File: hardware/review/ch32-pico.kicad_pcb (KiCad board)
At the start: 4 copper layers, 21 x 51 mm, 55 parts, among them J1 PICO 40-PIN, J2 GT-USB-7010AW, SW1 RESET, SW2 BOOT, U1 CH32X035C8T6, U3 TPS259470LRPWR, U4 AP63203WU-7

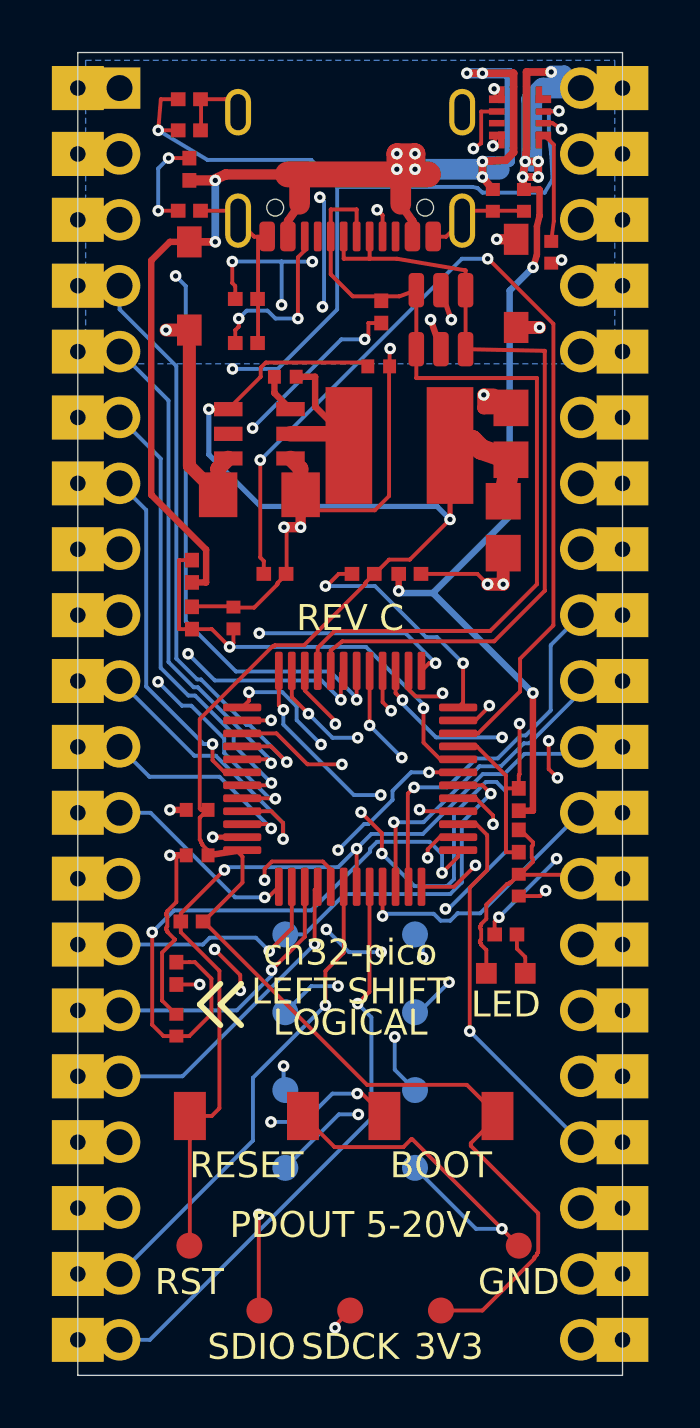
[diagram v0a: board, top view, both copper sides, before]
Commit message: Add pin 37 regulator enable control in Rev D
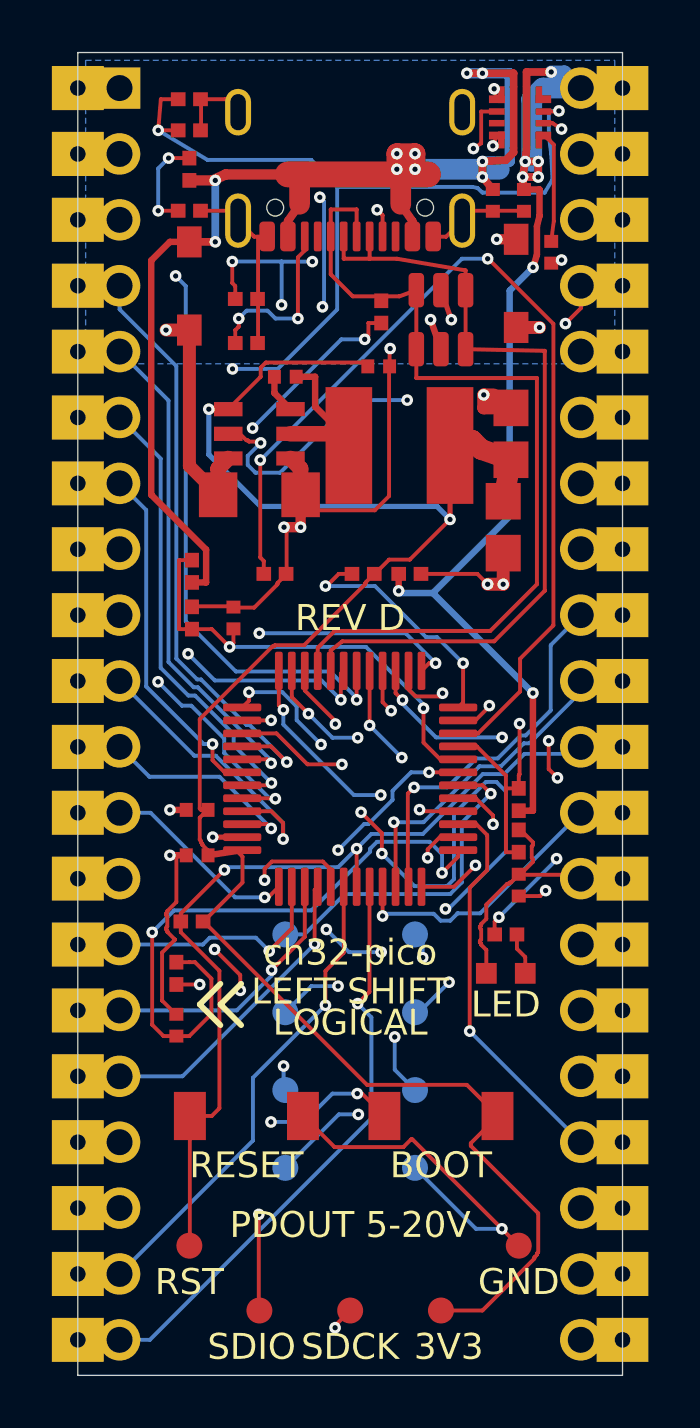
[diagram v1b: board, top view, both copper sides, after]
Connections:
- J1 pad 37: (no net) -> 3V3_EN
- U4 pad 2: (no net) -> 3V3_EN
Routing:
- net 3V3_EN: track 0.00 -> 18.9 mm, vias 0 -> 3
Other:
- board text added: "EN"
- board text added: "REV D"
- board text removed: "REV C"
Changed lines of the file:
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@@
 			(layers "*.Cu" "*.Mask")
 			(remove_unused_layers no)
+			(net "3V3_EN")
 		)
 		(pad "37" thru_hole rect
@@
 			(layers "*.Cu" "*.Mask")
 			(remove_unused_layers no)
+			(net "3V3_EN")
 		)
 		(pad "38" thru_hole circle
@@
 			(size 0.55 1.1)
 			(layers "F.Cu" "F.Mask" "F.Paste")
+			(net "3V3_EN")
 		)
 		(pad "3" smd rect
@@
 		)
 	)
-	(gr_text "REV C"
+	(gr_text "REV D"
 		(at 10.5 21.8 0)
 		(layer "F.SilkS")
@@
 		)
 	)
-	(gr_text "NC"
+	(gr_text "EN"
 		(at 16.6 8.99 0)
 		(layer "B.SilkS")
@@
 	)
 	(segment
+		(start 18.8 10.45)
+		(end 19.4 9.85)
+		(width 0.15)
+		(layer "F.Cu")
+		(net "3V3_EN")
+	)
+	(segment
+		(start 5.95 14.55)
+		(end 6.1 14.55)
+		(width 0.15)
+		(layer "F.Cu")
+		(net "3V3_EN")
+	)
+	(segment
+		(start 6.5 14.95)
+		(end 6.55 14.95)
+		(width 0.15)
+		(layer "F.Cu")
+		(net "3V3_EN")
+	)
+	(segment
+		(start 19.4 9.85)
+		(end 19.4 9)
+		(width 0.15)
+		(layer "F.Cu")
+		(net "3V3_EN")
+	)
+	(segment
+		(start 6.1 14.55)
+		(end 6.5 14.95)
+		(width 0.15)
+		(layer "F.Cu")
+		(net "3V3_EN")
+	)
+	(segment
+		(start 6.55 14.95)
+		(end 6.6 15)
+		(width 0.15)
+		(layer "F.Cu")
+		(net "3V3_EN")
+	)
+	(segment
+		(start 6.6 15)
+		(end 7 15)
+		(width 0.15)
+		(layer "F.Cu")
+		(net "3V3_EN")
+	)
+	(segment
+		(start 5.8 14.7)
+		(end 5.95 14.55)
+		(width 0.15)
+		(layer "F.Cu")
+		(net "3V3_EN")
+	)
+	(via
+		(at 12.7 13.4)
+		(size 0.45)
+		(drill 0.2)
+		(layers "F.Cu" "B.Cu")
+		(net "3V3_EN")
+	)
+	(via
+		(at 18.8 10.45)
+		(size 0.45)
+		(drill 0.2)
+		(layers "F.Cu" "B.Cu")
+		(net "3V3_EN")
+	)
+	(via
+		(at 7.05 15.05)
+		(size 0.45)
+		(drill 0.2)
+		(layers "F.Cu" "B.Cu")
+		(net "3V3_EN")
+	)
+	(segment
+		(start 7.8 16.2)
+		(end 10.6 13.4)
+		(width 0.15)
+		(layer "B.Cu")
+		(net "3V3_EN")
+	)
+	(segment
+		(start 10.6 13.4)
+		(end 12.7 13.4)
+		(width 0.15)
+		(layer "B.Cu")
+		(net "3V3_EN")
+	)
+	(segment
+		(start 6.85 16.2)
+		(end 7.8 16.2)
+		(width 0.15)
+		(layer "B.Cu")
+		(net "3V3_EN")
+	)
+	(segment
+		(start 6.55 15.55)
+		(end 6.55 15.9)
+		(width 0.15)
+		(layer "B.Cu")
+		(net "3V3_EN")
+	)
+	(segment
+		(start 7.05 15.05)
+		(end 6.55 15.55)
+		(width 0.15)
+		(layer "B.Cu")
+		(net "3V3_EN")
+	)
+	(segment
+		(start 6.55 15.9)
+		(end 6.85 16.2)
+		(width 0.15)
+		(layer "B.Cu")
+		(net "3V3_EN")
+	)
+	(segment
+		(start 14.2 12)
+		(end 17.25 12)
+		(width 0.15)
+		(layer "In2.Cu")
+		(net "3V3_EN")
+	)
+	(segment
+		(start 17.25 12)
+		(end 18.8 10.45)
+		(width 0.15)
+		(layer "In2.Cu")
+		(net "3V3_EN")
+	)
+	(segment
+		(start 12.8 13.4)
+		(end 14.2 12)
+		(width 0.15)
+		(layer "In2.Cu")
+		(net "3V3_EN")
+	)
+	(segment

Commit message: Expose Rev E diagnostics and build JLCPCB files with uv and just
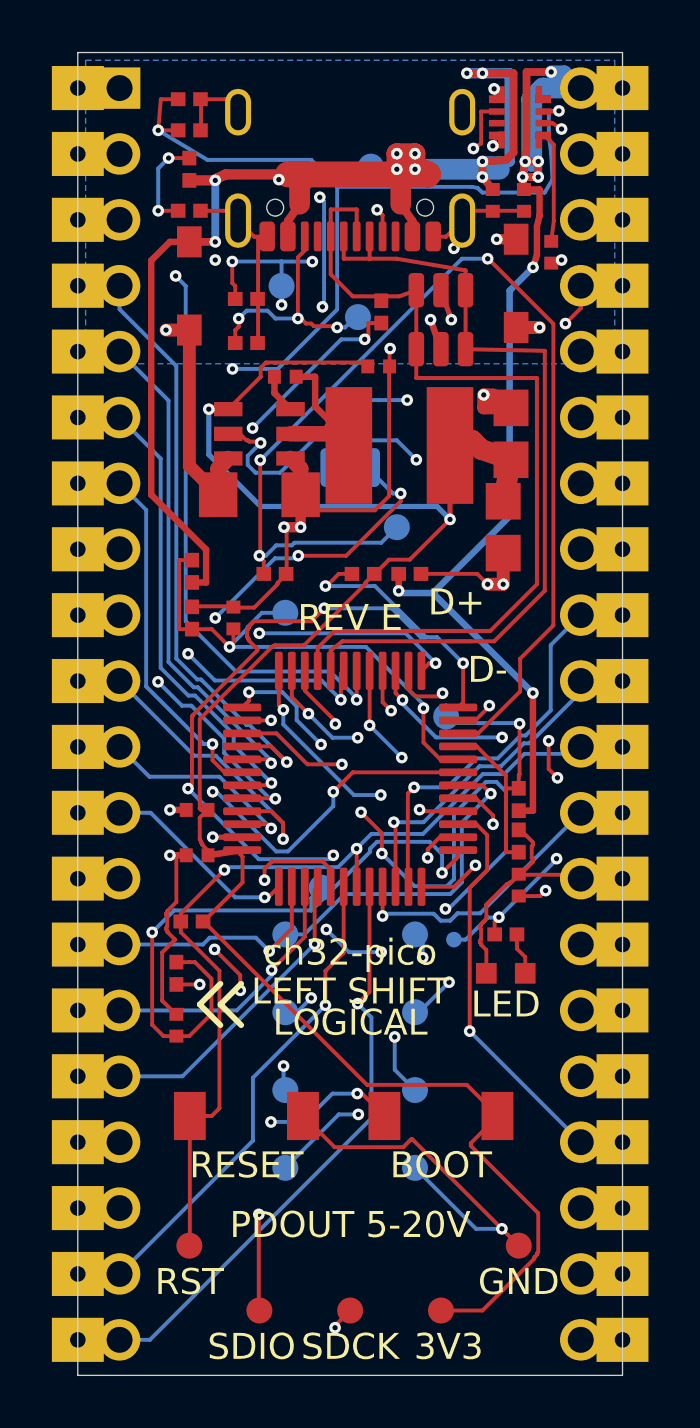
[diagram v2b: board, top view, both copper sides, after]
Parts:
- added SJ1: PC7 OPTION, ch32-pico:SolderJumper_Open, B.Cu at (10.5, 16.0)
- added TP14: CURRENT_SENSE, ch32-pico:TestPad_1mm, B.Cu at (9.40, 32.2)
- added TP15: VBUS, ch32-pico:TestPad_1mm, B.Cu at (8.60, 4.90)
- added TP16: GND, ch32-pico:TestPad_1mm, B.Cu at (11.3, 4.40)
- added TP17: VBUS_SENSE, ch32-pico:TestPad_1mm, B.Cu at (8.00, 21.6)
- added TP18: PDOUT_SENSE, ch32-pico:TestPad_1mm, B.Cu at (14.2, 25.6)
- added TP19: CC1, ch32-pico:TestPad_1mm, B.Cu at (7.86, 9.00)
- added TP20: CC2, ch32-pico:TestPad_1mm, B.Cu at (10.8, 10.2)
- added TP21: PD_ENABLE, ch32-pico:TestPad_1mm, B.Cu at (12.3, 18.3)
- added TP22: STATUS_LED, ch32-pico:TestPad_0.6mm, B.Cu at (14.5, 34.2)
- added TP23: USB_DP, ch32-pico:USB_Probe_Inline, F.Cu at (13.8, 22.3)
- added TP24: USB_DM, ch32-pico:USB_Probe_Inline, F.Cu at (14.7, 22.7)
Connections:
- J1 pad 35: (no net) -> GPIO35
- TP7 pad 1: PC7 -> PD_FAULT_N
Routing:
- net PD_FAULT_N: track 34.2 -> 63.4 mm, vias 5 -> 9
- net PC7: track 13.8 -> 30.1 mm, vias 3 -> 5
- net GPIO35: track 0.00 -> 10.8 mm, vias 0 -> 1
- net PD_ENABLE: track 45.6 -> 51.5 mm, vias 3 -> 4
- net PDOUT_SENSE: track 16.7 -> 19.7 mm
- net VBUS_SENSE: track 17.6 -> 20.3 mm
- net CC2: track 29.9 -> 32.5 mm, vias 3 -> 4
- net STATUS_LED: track 13.2 -> 15.3 mm
- net VBUS: track 54.0 -> 55.8 mm, vias 10 -> 11
- net CURRENT_SENSE: track 24.1 -> 25.1 mm
- net CC1: track 28.0 -> 28.7 mm
- net GND: vias 13 -> 15
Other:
- board text added: "CC1"
- board text added: "CC2"
- board text added: "D+"
- board text added: "D-"
- board text added: "FAULT"
- board text added: "ISNS"
- board text added: "OSNS"
- board text added: "PB3"
- board text added: "PC7*"
- board text added: "PDEN"
- board text added: "REV E"
- board text added: "SJ1"
- board text added: "VBUS"
- board text added: "VSNS"
- board text removed: "NC"
- board text removed: "PC7"
- board text removed: "REV D"

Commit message: Fix power component ratings and assembly placement metadata
Use verified 50 V bypass capacitors, reduce the nominal eFuse limit to 2.93 A, and validate BOM metadata against the reviewed board. Apply JLC model frame corrections and extend regression coverage.

Record the parts inventory, exact-MCU sourcing options, and unresolved power qualification requirements. Retain CH32X035C8T6 and its GPIO allocation.
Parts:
- R17: value 1k -> 4.7k
- TP7: value PC7 -> PD_FAULT_N
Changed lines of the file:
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@@
 			)
 		)
-		(property "LCSC Part" "C52923"
+		(property "LCSC Part" "C307331"
 			(at 0 0 90)
 			(layer "F.Fab")
@@
 			)
 		)
-		(property "LCSC Part" "C25900"
+		(property "LCSC Part" "C25744"
 			(at 0 0 0)
 			(layer "F.Fab")
@@
 			)
 		)
-		(property "LCSC Part" "C25900"
+		(property "LCSC Part" "C25741"
 			(at 0 0 90)
 			(layer "F.Fab")
@@
 			)
 		)
-		(property "LCSC Part" "C52923"
+		(property "LCSC Part" "C307331"
 			(at 0 0 180)
 			(layer "F.Fab")
@@
 			)
 		)
-		(property "LCSC Part" "C25900"
+		(property "LCSC Part" "C25744"
 			(at 0 0 0)
 			(layer "F.Fab")
@@
 			)
 		)
-		(property "LCSC Part" "C52923"
+		(property "LCSC Part" "C307331"
 			(at 0 0 90)
 			(layer "F.Fab")
@@
 			)
 		)
-		(property "Value" "1k"
+		(property "Value" "4.7k"
 			(at 0 4 0)
 			(layer "F.Fab")
@@
 			)
 		)
-		(property "LCSC Part" "C52923"
+		(property "LCSC Part" "C307331"
 			(at 0 0 270)
 			(layer "F.Fab")
@@
 			)
 		)
-		(property "LCSC Part" "C25900"
+		(property "LCSC Part" "C25744"
 			(at 0 0 0)
 			(layer "F.Fab")
@@
 			)
 		)
-		(property "LCSC Part" "C25900"
+		(property "LCSC Part" "C25744"
 			(at 0 0 0)
 			(layer "F.Fab")
@@
 			)
 		)
+		(property "LCSC Part" "C3662793"
+			(at 0 0 0)
+			(layer "F.Fab")
+			(hide yes)
+			(effects
+				(font
+					(size 1.27 1.27)
+					(thickness 0.15)
+				)
+			)
+		)
 		(attr smd)
 		(duplicate_pad_numbers_are_jumpers no)
@@
 			)
 		)
-		(property "LCSC Part" "C25900"
+		(property "LCSC Part" "C11702"
 			(at 0 0 90)
 			(layer "F.Fab")
@@
 			)
 		)
-		(property "LCSC Part" "C52923"
+		(property "LCSC Part" "C307331"
 			(at 0 0 90)
 			(layer "F.Fab")
@@
 			)
 		)
-		(property "LCSC Part" "C25900"
+		(property "LCSC Part" "C25905"
 			(at 0 0 0)
 			(layer "F.Fab")
@@
 			)
 		)
-		(property "LCSC Part" "C25900"
+		(property "LCSC Part" "C25905"
 			(at 0 0 0)
 			(layer "F.Fab")
@@
 			)
 		)
-		(property "LCSC Part" "C25900"
+		(property "LCSC Part" "C25744"
 			(at 0 0 90)
 			(layer "F.Fab")
@@
 			)
 		)
-		(property "LCSC Part" "C25900"
+		(property "LCSC Part" "C11702"
 			(at 0 0 0)
 			(layer "F.Fab")
@@
 			)
 		)
-		(property "LCSC Part" "C52923"
+		(property "LCSC Part" "C307331"
 			(at 0 0 270)
 			(layer "F.Fab")
@@
 			)
 		)
-		(property "LCSC Part" "C52923"
+		(property "LCSC Part" "C307331"
 			(at 0 0 0)
 			(layer "F.Fab")
@@
 			)
 		)
-		(property "LCSC Part" "C52923"
+		(property "LCSC Part" "C307331"
 			(at 0 0 0)
 			(layer "F.Fab")
@@
 			)
 		)
+		(property "LCSC Part" "C7519"
+			(at 0 2.4 90)
+			(layer "F.Fab")
+			(hide yes)
+			(effects
+				(font
+					(size 1 1)
+					(thickness 0.15)
+				)
+			)
+		)
 		(attr smd)
 		(duplicate_pad_numbers_are_jumpers no)
@@
 			)
 		)
-		(property "LCSC Part" "C25900"
+		(property "LCSC Part" "C25744"
 			(at 0 0 90)
 			(layer "F.Fab")
@@
 			)
 		)
-		(property "LCSC Part" "C25900"
+		(property "LCSC Part" "C4142"
 			(at 0 0 90)
 			(layer "F.Fab")
@@
 			)
 		)
-		(property "LCSC Part" "C52923"
+		(property "LCSC Part" "C307331"
 			(at 0 0 270)
 			(layer "F.Fab")
@@
 			)
 		)
-		(property "LCSC Part" "C25900"
+		(property "LCSC Part" "C25741"
 			(at 0 0 90)
 			(layer "F.Fab")
@@
 			)
 		)
+		(property "LCSC Part" "C963411"
+			(at 0 5 180)
+			(layer "F.Fab")
+			(hide yes)
+			(effects
+				(font
+					(size 1 1)
+					(thickness 0.15)
+				)
+			)
+		)
 		(attr smd)
 		(duplicate_pad_numbers_are_jumpers no)
@@
 			)
 		)
+		(property "LCSC Part" "C29779902"
+			(at 0 5.85 90)
+			(layer "F.Fab")
+			(hide yes)
+			(effects
+				(font
+					(size 1 1)
+					(thickness 0.15)
+				)
+			)
+		)
 		(attr smd)
 		(duplicate_pad_numbers_are_jumpers no)
@@
 			)
 		)
-		(property "LCSC Part" "C25900"
+		(property "LCSC Part" "C25867"
 			(at 0 0 0)
 			(layer "F.Fab")
@@
 			)
 		)
-		(property "Value" "PC7"
+		(property "Value" "PD_FAULT_N"
 			(at 0 1.2 0)
 			(layer "B.Fab")
